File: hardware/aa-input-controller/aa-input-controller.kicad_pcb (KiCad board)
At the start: 2 copper layers, 95.4 x 54 mm, 65 parts, among them CN101 Conn_01x02, CN201 INPUT, CN202 Connector_Sony_Playstation_Du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, CN203 Conn_01x06_Male, CN211 BTN_R, CN221 BTN_G, CN231 BTN_B, CN241 BTN_P, CN251 Conn_01x06_Male, Q211 MCH3484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

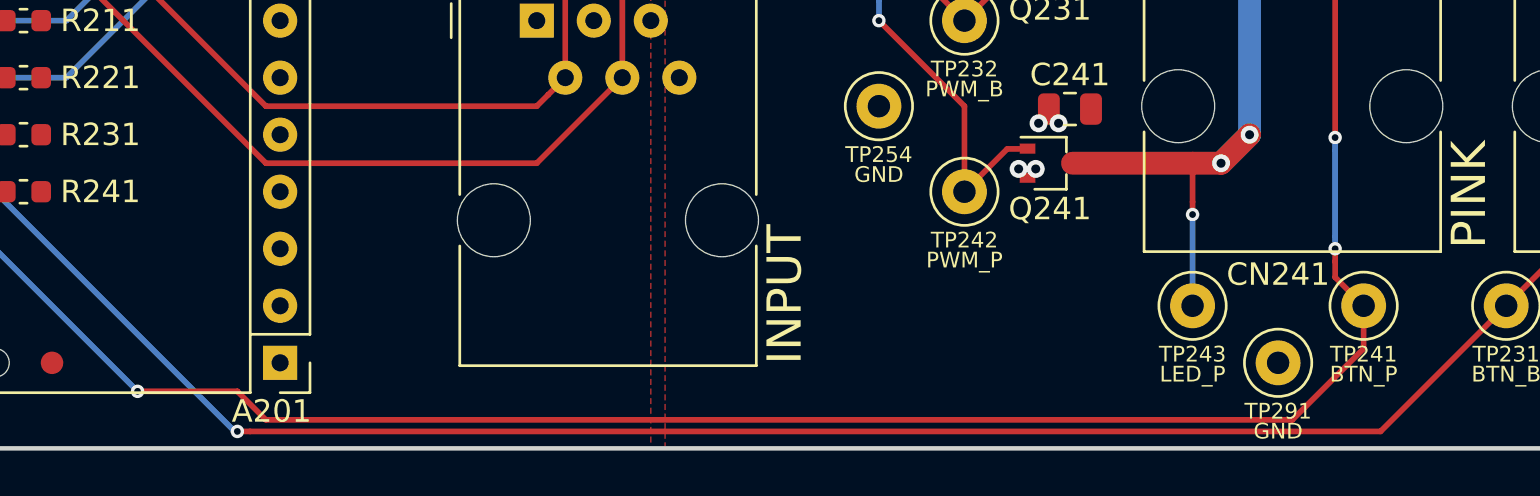
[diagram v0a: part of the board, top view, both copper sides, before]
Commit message: Minor board updates to fix issues discovered during build
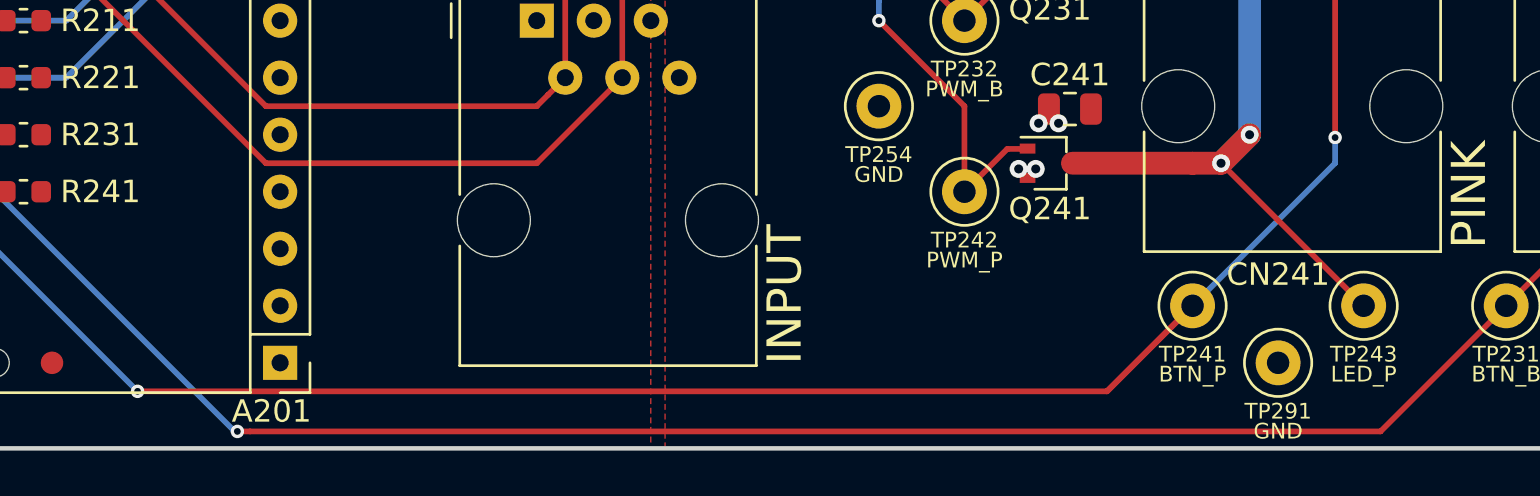
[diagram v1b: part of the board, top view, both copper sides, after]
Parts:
- R211, R221, R231, R241: value 4.7k -> 1k
- moved TP241 7.62 mm to (166.4, 120.7)
- moved TP243 7.62 mm to (174.0, 120.7)
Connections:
- A201 pad 38: Net-(A201-Pad38) -> +5V
- A201 pad 40: +5V -> Net-(A201-Pad40)
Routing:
- net /BTN_P: track 92.3 -> 89.5 mm, vias 3 -> 2
- net /LED_DRIVE_P: track 26.7 -> 29.4 mm, vias 3 -> 2
